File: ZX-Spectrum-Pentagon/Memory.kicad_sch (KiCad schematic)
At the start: 10 parts

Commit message: prepare for pcb
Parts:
- U31: value (none) -> 74HC32; footprint (none) -> Package_DIP:DIP-14_W7.62mm
- U34, U49: value (none) -> 74HC08; footprint (none) -> Package_DIP:DIP-14_W7.62mm
- U42, U46, U47, U48: value (none) -> 74HC257; footprint (none) -> Package_DIP:DIP-16_W7.62mm
- U43: value (none) -> 74HC541; footprint (none) -> Package_DIP:DIP-20_W7.62mm
- U44: value (none) -> HM628512; footprint (none) -> Package_DIP:DIP-32_W15.24mm
- U45: value (none) -> 74HC574; footprint (none) -> Package_DIP:DIP-20_W7.62mm
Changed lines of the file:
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@@
     (in_bom yes) (on_board yes)
     (property "Reference" "U44" (id 0) (at 109.22 20.32 0))
-    (property "Value" "" (id 1) (at 109.22 78.74 0))
-    (property "Footprint" "" (id 2) (at 109.22 20.32 0)
+    (property "Value" "HM628512" (id 1) (at 109.22 78.74 0))
+    (property "Footprint" "Package_DIP:DIP-32_W15.24mm" (id 2) (at 109.22 20.32 0)
       (effects (font (size 1.27 1.27)) hide)
     )
@@
     (in_bom yes) (on_board yes)
     (property "Reference" "U31" (id 0) (at 71.12 162.56 0))
-    (property "Value" "" (id 1) (at 71.12 170.18 0))
-    (property "Footprint" "" (id 2) (at 71.12 173.99 0)
+    (property "Value" "74HC32" (id 1) (at 71.12 170.18 0))
+    (property "Footprint" "Package_DIP:DIP-14_W7.62mm" (id 2) (at 71.12 173.99 0)
       (effects (font (size 1.27 1.27)) hide)
     )
@@
     (in_bom yes) (on_board yes)
     (property "Reference" "U43" (id 0) (at 146.05 21.59 0))
-    (property "Value" "" (id 1) (at 146.05 52.07 0))
-    (property "Footprint" "" (id 2) (at 146.05 21.59 0)
+    (property "Value" "74HC541" (id 1) (at 146.05 52.07 0))
+    (property "Footprint" "Package_DIP:DIP-20_W7.62mm" (id 2) (at 146.05 21.59 0)
       (effects (font (size 1.27 1.27)) hide)
     )
@@
     (in_bom yes) (on_board yes)
     (property "Reference" "U42" (id 0) (at 58.42 19.05 0))
-    (property "Value" "" (id 1) (at 58.42 46.99 0))
-    (property "Footprint" "" (id 2) (at 72.39 31.75 0)
+    (property "Value" "74HC257" (id 1) (at 58.42 46.99 0))
+    (property "Footprint" "Package_DIP:DIP-16_W7.62mm" (id 2) (at 72.39 31.75 0)
       (effects (font (size 1.27 1.27)) hide)
     )
@@
     (in_bom yes) (on_board yes)
     (property "Reference" "U46" (id 0) (at 58.42 57.15 0))
-    (property "Value" "" (id 1) (at 58.42 85.09 0))
-    (property "Footprint" "" (id 2) (at 72.39 69.85 0)
+    (property "Value" "74HC257" (id 1) (at 58.42 85.09 0))
+    (property "Footprint" "Package_DIP:DIP-16_W7.62mm" (id 2) (at 72.39 69.85 0)
       (effects (font (size 1.27 1.27)) hide)
     )
@@
     (in_bom yes) (on_board yes)
     (property "Reference" "U47" (id 0) (at 58.42 95.25 0))
-    (property "Value" "" (id 1) (at 58.42 123.19 0))
-    (property "Footprint" "" (id 2) (at 72.39 107.95 0)
+    (property "Value" "74HC257" (id 1) (at 58.42 123.19 0))
+    (property "Footprint" "Package_DIP:DIP-16_W7.62mm" (id 2) (at 72.39 107.95 0)
       (effects (font (size 1.27 1.27)) hide)
     )
@@
     (in_bom yes) (on_board yes)
     (property "Reference" "U48" (id 0) (at 58.42 133.35 0))
-    (property "Value" "" (id 1) (at 58.42 161.29 0))
-    (property "Footprint" "" (id 2) (at 72.39 146.05 0)
+    (property "Value" "74HC257" (id 1) (at 58.42 161.29 0))
+    (property "Footprint" "Package_DIP:DIP-16_W7.62mm" (id 2) (at 72.39 146.05 0)
       (effects (font (size 1.27 1.27)) hide)
     )
@@
     (in_bom yes) (on_board yes)
     (property "Reference" "U45" (id 0) (at 146.05 54.61 0))
-    (property "Value" "" (id 1) (at 146.05 82.55 0))
-    (property "Footprint" "" (id 2) (at 146.05 76.2 0)
+    (property "Value" "74HC574" (id 1) (at 146.05 82.55 0))
+    (property "Footprint" "Package_DIP:DIP-20_W7.62mm" (id 2) (at 146.05 76.2 0)
       (effects (font (size 1.27 1.27)) hide)
     )
@@
     (in_bom yes) (on_board yes)
     (property "Reference" "U34" (id 0) (at 71.12 172.72 0))
-    (property "Value" "" (id 1) (at 71.12 180.34 0))
-    (property "Footprint" "" (id 2) (at 71.12 184.15 0)
+    (property "Value" "74HC08" (id 1) (at 71.12 180.34 0))
+    (property "Footprint" "Package_DIP:DIP-14_W7.62mm" (id 2) (at 71.12 184.15 0)
       (effects (font (size 1.27 1.27)) hide)
     )
@@
     (in_bom yes) (on_board yes)
     (property "Reference" "U49" (id 0) (at 71.12 182.88 0))
-    (property "Value" "" (id 1) (at 71.12 190.5 0))
-    (property "Footprint" "" (id 2) (at 71.12 194.31 0)
+    (property "Value" "74HC08" (id 1) (at 71.12 190.5 0))
+    (property "Footprint" "Package_DIP:DIP-14_W7.62mm" (id 2) (at 71.12 194.31 0)
       (effects (font (size 1.27 1.27)) hide)
     )
@@
     (in_bom yes) (on_board yes)
     (property "Reference" "U34" (id 0) (at 54.61 171.45 0))
-    (property "Value" "" (id 1) (at 54.61 179.07 0))
-    (property "Footprint" "" (id 2) (at 54.61 182.88 0)
-      (effects (font (size 1.27 1.27)) hide)
-    )
+    (property "Value" "74HC08" (id 1) (at 54.61 179.07 0))
+    (property "Footprint" "Package_DIP:DIP-14_W7.62mm" (id 2) (at 54.61 182.88 0)
+      (effects (font (size 1.27 1.27)) hide)
+    )

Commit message: clear annotate
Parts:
- renumbered U44 to U?, U31 to U?, U43 to U?, U42 to U?, U46 to U?, U47 to U?, U48 to U?, U45 to U?, U34 to U?, U49 to U?
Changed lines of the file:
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@@
   (symbol (lib_id "GenericSRAM:HM628512") (at 109.22 49.53 0) (unit 1)
     (in_bom yes) (on_board yes)
-    (property "Reference" "U44" (id 0) (at 109.22 20.32 0))
+    (property "Reference" "U?" (id 0) (at 109.22 20.32 0))
     (property "Value" "HM628512" (id 1) (at 109.22 78.74 0))
     (property "Footprint" "Package_DIP:DIP-32_W15.24mm" (id 2) (at 109.22 20.32 0)
@@
   (symbol (lib_id "power:GND") (at 30.48 185.42 270) (mirror x) (unit 1)
     (in_bom yes) (on_board yes)
-    (property "Reference" "#PWR0158" (id 0) (at 24.13 185.42 0)
+    (property "Reference" "#PWR?" (id 0) (at 24.13 185.42 0)
       (effects (font (size 1.27 1.27)) hide)
     )
@@
   (symbol (lib_id "power:VCC") (at 30.48 187.96 90) (mirror x) (unit 1)
     (in_bom yes) (on_board yes)
-    (property "Reference" "#PWR0159" (id 0) (at 34.29 187.96 0)
+    (property "Reference" "#PWR?" (id 0) (at 34.29 187.96 0)
       (effects (font (size 1.27 1.27)) hide)
     )
@@
   (symbol (lib_id "74IEC:74HC32") (at 71.12 166.37 0) (unit 4)
     (in_bom yes) (on_board yes)
-    (property "Reference" "U31" (id 0) (at 71.12 162.56 0))
+    (property "Reference" "U?" (id 0) (at 71.12 162.56 0))
     (property "Value" "74HC32" (id 1) (at 71.12 170.18 0))
     (property "Footprint" "Package_DIP:DIP-14_W7.62mm" (id 2) (at 71.12 173.99 0)
@@
   (symbol (lib_id "74IEC:74HC541") (at 146.05 35.56 0) (unit 1)
     (in_bom yes) (on_board yes)
-    (property "Reference" "U43" (id 0) (at 146.05 21.59 0))
+    (property "Reference" "U?" (id 0) (at 146.05 21.59 0))
     (property "Value" "74HC541" (id 1) (at 146.05 52.07 0))
     (property "Footprint" "Package_DIP:DIP-20_W7.62mm" (id 2) (at 146.05 21.59 0)
@@
   (symbol (lib_id "74IEC:74HC257") (at 58.42 33.02 0) (unit 1)
     (in_bom yes) (on_board yes)
-    (property "Reference" "U42" (id 0) (at 58.42 19.05 0))
+    (property "Reference" "U?" (id 0) (at 58.42 19.05 0))
     (property "Value" "74HC257" (id 1) (at 58.42 46.99 0))
     (property "Footprint" "Package_DIP:DIP-16_W7.62mm" (id 2) (at 72.39 31.75 0)
@@
   (symbol (lib_id "74IEC:74HC257") (at 58.42 71.12 0) (unit 1)
     (in_bom yes) (on_board yes)
-    (property "Reference" "U46" (id 0) (at 58.42 57.15 0))
+    (property "Reference" "U?" (id 0) (at 58.42 57.15 0))
     (property "Value" "74HC257" (id 1) (at 58.42 85.09 0))
     (property "Footprint" "Package_DIP:DIP-16_W7.62mm" (id 2) (at 72.39 69.85 0)
@@
   (symbol (lib_id "74IEC:74HC257") (at 58.42 109.22 0) (unit 1)
     (in_bom yes) (on_board yes)
-    (property "Reference" "U47" (id 0) (at 58.42 95.25 0))
+    (property "Reference" "U?" (id 0) (at 58.42 95.25 0))
     (property "Value" "74HC257" (id 1) (at 58.42 123.19 0))
     (property "Footprint" "Package_DIP:DIP-16_W7.62mm" (id 2) (at 72.39 107.95 0)
@@
   (symbol (lib_id "74IEC:74HC257") (at 58.42 147.32 0) (unit 1)
     (in_bom yes) (on_board yes)
-    (property "Reference" "U48" (id 0) (at 58.42 133.35 0))
+    (property "Reference" "U?" (id 0) (at 58.42 133.35 0))
     (property "Value" "74HC257" (id 1) (at 58.42 161.29 0))
     (property "Footprint" "Package_DIP:DIP-16_W7.62mm" (id 2) (at 72.39 146.05 0)
@@
   (symbol (lib_id "74IEC:74HC574") (at 146.05 68.58 0) (unit 1)
     (in_bom yes) (on_board yes)
-    (property "Reference" "U45" (id 0) (at 146.05 54.61 0))
+    (property "Reference" "U?" (id 0) (at 146.05 54.61 0))
     (property "Value" "74HC574" (id 1) (at 146.05 82.55 0))
     (property "Footprint" "Package_DIP:DIP-20_W7.62mm" (id 2) (at 146.05 76.2 0)
@@
   (symbol (lib_id "74IEC:74HC08") (at 71.12 176.53 0) (unit 4)
     (in_bom yes) (on_board yes)
-    (property "Reference" "U34" (id 0) (at 71.12 172.72 0))
+    (property "Reference" "U?" (id 0) (at 71.12 172.72 0))
     (property "Value" "74HC08" (id 1) (at 71.12 180.34 0))
     (property "Footprint" "Package_DIP:DIP-14_W7.62mm" (id 2) (at 71.12 184.15 0)
@@
   (symbol (lib_id "74IEC:74HC08") (at 71.12 186.69 0) (unit 1)
     (in_bom yes) (on_board yes)
-    (property "Reference" "U49" (id 0) (at 71.12 182.88 0))
+    (property "Reference" "U?" (id 0) (at 71.12 182.88 0))
     (property "Value" "74HC08" (id 1) (at 71.12 190.5 0))
     (property "Footprint" "Package_DIP:DIP-14_W7.62mm" (id 2) (at 71.12 194.31 0)
@@
   (symbol (lib_id "74IEC:74HC08") (at 54.61 175.26 0) (unit 3)
     (in_bom yes) (on_board yes)
-    (property "Reference" "U34" (id 0) (at 54.61 171.45 0))
+    (property "Reference" "U?" (id 0) (at 54.61 171.45 0))
     (property "Value" "74HC08" (id 1) (at 54.61 179.07 0))
     (property "Footprint" "Package_DIP:DIP-14_W7.62mm" (id 2) (at 54.61 182.88 0)

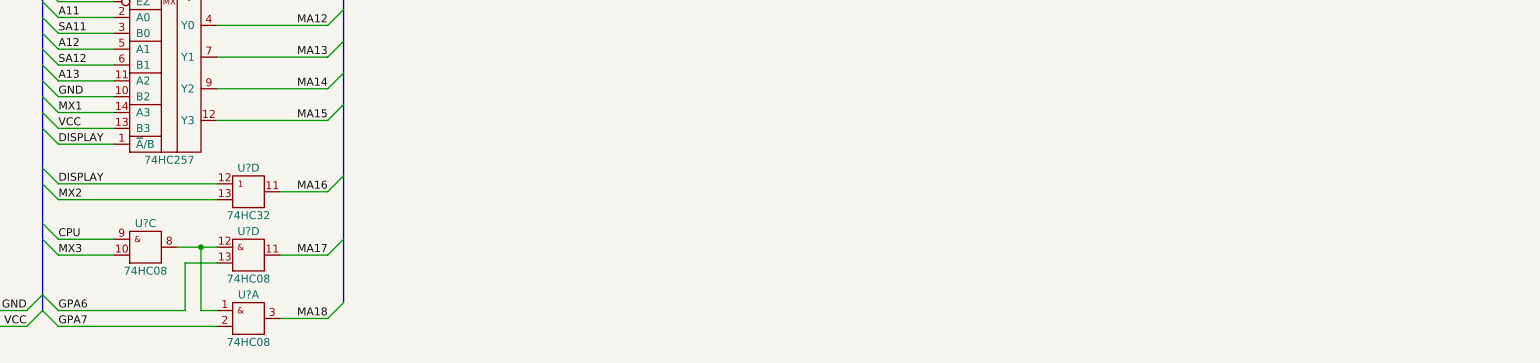
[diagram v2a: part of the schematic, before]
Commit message: reuse units of ic
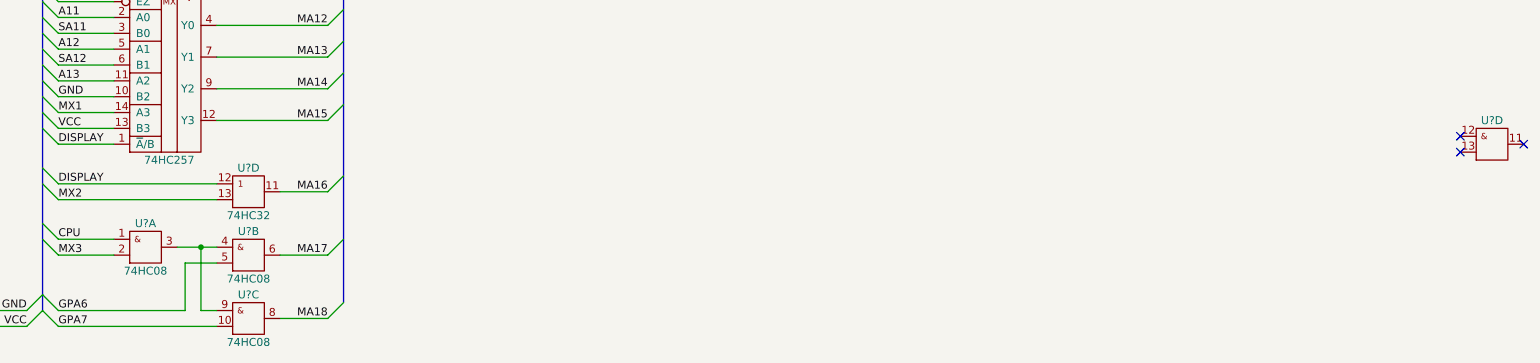
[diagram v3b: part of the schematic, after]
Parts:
- added U?: ~, symbol 74IEC:74HC08
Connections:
- net CPU: now also U?.1 (A); no longer U?.9 (A)
- net GND: now also U?.7 (GND)
- net GPA6: now also U?.5 (B); no longer U?.13 (B)
- net GPA7: now also U?.10 (B); no longer U?.2 (B)
- net MA17: now also U?.6 (~{Y}); no longer U?.11 (~{Y})
- net MA18: now also U?.8 (~{Y}); no longer U?.3 (~{Y})
- net MX3: now also U?.2 (B); no longer U?.10 (B)
- net VCC: now also U?.14 (VCC)
- new net: U?.3 (~{Y}), U?.4 (A), U?.9 (A)
- no-connect marks 0 -> 3
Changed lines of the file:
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@@
   (junction (at 127 13.97) (diameter 0) (color 0 0 0 0)
   )
+  (no_connect (at 265.43 160.02))
+  (no_connect (at 275.59 158.75))
+  (no_connect (at 265.43 157.48))
   (bus_entry (at 38.1 135.89) (size 2.54 2.54)
     (stroke (width 0) (type default) (color 0 0 0 0))
@@
     (pin "9")
   )
-  (symbol (lib_id "74IEC:74HC08") (at 71.12 176.53 0) (unit 4)
+  (symbol (lib_id "74IEC:74HC08") (at 71.12 176.53 0) (unit 2)
     (in_bom yes) (on_board yes)
     (property "Reference" "U?" (id 0) (at 71.12 172.72 0))
@@
     (pin "13")
   )
-  (symbol (lib_id "74IEC:74HC08") (at 71.12 186.69 0) (unit 1)
+  (symbol (lib_id "74IEC:74HC08") (at 71.12 186.69 0) (unit 3)
     (in_bom yes) (on_board yes)
     (property "Reference" "U?" (id 0) (at 71.12 182.88 0))
@@
     (pin "13")
   )
-  (symbol (lib_id "74IEC:74HC08") (at 54.61 175.26 0) (unit 3)
+  (symbol (lib_id "74IEC:74HC08") (at 54.61 175.26 0) (unit 1)
     (in_bom yes) (on_board yes)
     (property "Reference" "U?" (id 0) (at 54.61 171.45 0))
@@
       (effects (font (size 1.27 1.27)) hide)
     )
+    (pin "14")
+    (pin "7")
+    (pin "1")
+    (pin "2")
+    (pin "3")
+    (pin "4")
+    (pin "5")
+    (pin "6")
+    (pin "10")
+    (pin "8")
+    (pin "9")
+    (pin "11")
+    (pin "12")
+    (pin "13")
+  )
+  (symbol (lib_id "74IEC:74HC08") (at 270.51 158.75 0) (unit 4)
+    (in_bom yes) (on_board no)
+    (property "Reference" "U?" (id 0) (at 270.51 154.94 0))
+    (property "Value" "~" (id 1) (at 270.51 162.56 0))
+    (property "Footprint" "" (id 2) (at 270.51 166.37 0)
+      (effects (font (size 1.27 1.27)) hide)
+    )
+    (property "Datasheet" "https://www.ti.com/lit/ug/scyd013b/scyd013b.pdf" (id 3) (at 270.51 154.94 0)
+      (effects (font (size 1.27 1.27)) hide)
+    )

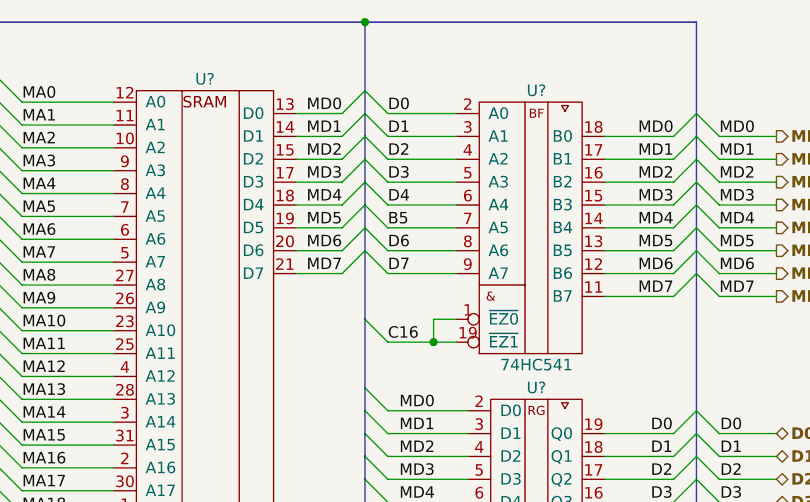
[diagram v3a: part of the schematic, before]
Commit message: revert data bus HC245 delete invertor for another direction fix line label
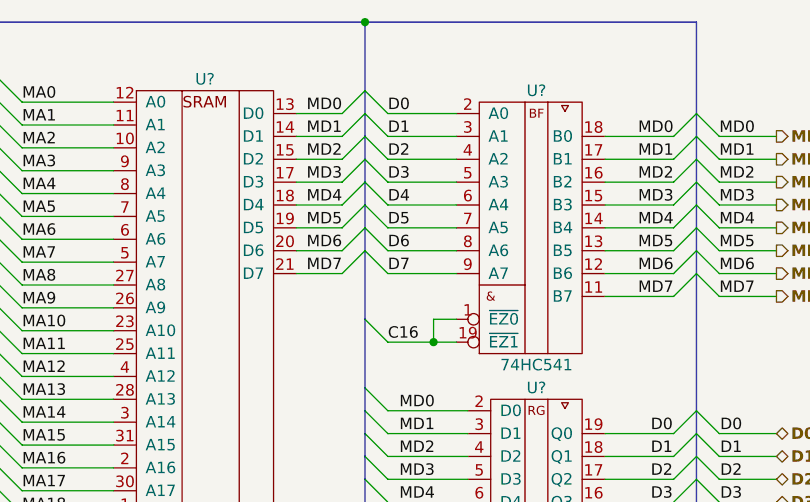
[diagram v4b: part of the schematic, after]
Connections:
- net В5 is gone; now on net D5: U?.7 (A5)
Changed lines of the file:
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@@
     (effects (font (size 1.27 1.27)) (justify left bottom))
   )
-  (label "В5" (at 129.54 36.83 0)
+  (label "D5" (at 129.54 36.83 0)
     (effects (font (size 1.27 1.27)) (justify left bottom))
   )

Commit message: annotate
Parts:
- gave numbers to parts that had none: 10
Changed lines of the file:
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@@
   (symbol (lib_id "GenericSRAM:HM628512") (at 109.22 49.53 0) (unit 1)
     (in_bom yes) (on_board yes)
-    (property "Reference" "U?" (id 0) (at 109.22 20.32 0))
+    (property "Reference" "U45" (id 0) (at 109.22 20.32 0))
     (property "Value" "HM628512" (id 1) (at 109.22 78.74 0))
     (property "Footprint" "Package_DIP:DIP-32_W15.24mm" (id 2) (at 109.22 20.32 0)
@@
   (symbol (lib_id "power:GND") (at 30.48 185.42 270) (mirror x) (unit 1)
     (in_bom yes) (on_board yes)
-    (property "Reference" "#PWR?" (id 0) (at 24.13 185.42 0)
+    (property "Reference" "#PWR059" (id 0) (at 24.13 185.42 0)
       (effects (font (size 1.27 1.27)) hide)
     )
@@
   (symbol (lib_id "power:VCC") (at 30.48 187.96 90) (mirror x) (unit 1)
     (in_bom yes) (on_board yes)
-    (property "Reference" "#PWR?" (id 0) (at 34.29 187.96 0)
+    (property "Reference" "#PWR060" (id 0) (at 34.29 187.96 0)
       (effects (font (size 1.27 1.27)) hide)
     )
@@
   (symbol (lib_id "74IEC:74HC32") (at 71.12 166.37 0) (unit 4)
     (in_bom yes) (on_board yes)
-    (property "Reference" "U?" (id 0) (at 71.12 162.56 0))
+    (property "Reference" "U31" (id 0) (at 71.12 162.56 0))
     (property "Value" "74HC32" (id 1) (at 71.12 170.18 0))
     (property "Footprint" "Package_DIP:DIP-14_W7.62mm" (id 2) (at 71.12 173.99 0)
@@
   (symbol (lib_id "74IEC:74HC541") (at 146.05 35.56 0) (unit 1)
     (in_bom yes) (on_board yes)
-    (property "Reference" "U?" (id 0) (at 146.05 21.59 0))
+    (property "Reference" "U44" (id 0) (at 146.05 21.59 0))
     (property "Value" "74HC541" (id 1) (at 146.05 52.07 0))
     (property "Footprint" "Package_DIP:DIP-20_W7.62mm" (id 2) (at 146.05 21.59 0)
@@
   (symbol (lib_id "74IEC:74HC257") (at 58.42 33.02 0) (unit 1)
     (in_bom yes) (on_board yes)
-    (property "Reference" "U?" (id 0) (at 58.42 19.05 0))
+    (property "Reference" "U43" (id 0) (at 58.42 19.05 0))
     (property "Value" "74HC257" (id 1) (at 58.42 46.99 0))
     (property "Footprint" "Package_DIP:DIP-16_W7.62mm" (id 2) (at 72.39 31.75 0)
@@
   (symbol (lib_id "74IEC:74HC257") (at 58.42 71.12 0) (unit 1)
     (in_bom yes) (on_board yes)
-    (property "Reference" "U?" (id 0) (at 58.42 57.15 0))
+    (property "Reference" "U47" (id 0) (at 58.42 57.15 0))
     (property "Value" "74HC257" (id 1) (at 58.42 85.09 0))
     (property "Footprint" "Package_DIP:DIP-16_W7.62mm" (id 2) (at 72.39 69.85 0)
@@
   (symbol (lib_id "74IEC:74HC257") (at 58.42 109.22 0) (unit 1)
     (in_bom yes) (on_board yes)
-    (property "Reference" "U?" (id 0) (at 58.42 95.25 0))
+    (property "Reference" "U48" (id 0) (at 58.42 95.25 0))
     (property "Value" "74HC257" (id 1) (at 58.42 123.19 0))
     (property "Footprint" "Package_DIP:DIP-16_W7.62mm" (id 2) (at 72.39 107.95 0)
@@
   (symbol (lib_id "74IEC:74HC257") (at 58.42 147.32 0) (unit 1)
     (in_bom yes) (on_board yes)
-    (property "Reference" "U?" (id 0) (at 58.42 133.35 0))
+    (property "Reference" "U49" (id 0) (at 58.42 133.35 0))
     (property "Value" "74HC257" (id 1) (at 58.42 161.29 0))
     (property "Footprint" "Package_DIP:DIP-16_W7.62mm" (id 2) (at 72.39 146.05 0)
@@
   (symbol (lib_id "74IEC:74HC574") (at 146.05 68.58 0) (unit 1)
     (in_bom yes) (on_board yes)
-    (property "Reference" "U?" (id 0) (at 146.05 54.61 0))
+    (property "Reference" "U46" (id 0) (at 146.05 54.61 0))
     (property "Value" "74HC574" (id 1) (at 146.05 82.55 0))
     (property "Footprint" "Package_DIP:DIP-20_W7.62mm" (id 2) (at 146.05 76.2 0)
@@
   (symbol (lib_id "74IEC:74HC08") (at 71.12 176.53 0) (unit 2)
     (in_bom yes) (on_board yes)
-    (property "Reference" "U?" (id 0) (at 71.12 172.72 0))
+    (property "Reference" "U51" (id 0) (at 71.12 172.72 0))
     (property "Value" "74HC08" (id 1) (at 71.12 180.34 0))
     (property "Footprint" "Package_DIP:DIP-14_W7.62mm" (id 2) (at 71.12 184.15 0)
@@
   (symbol (lib_id "74IEC:74HC08") (at 71.12 186.69 0) (unit 3)
     (in_bom yes) (on_board yes)
-    (property "Reference" "U?" (id 0) (at 71.12 182.88 0))
+    (property "Reference" "U51" (id 0) (at 71.12 182.88 0))
     (property "Value" "74HC08" (id 1) (at 71.12 190.5 0))
     (property "Footprint" "Package_DIP:DIP-14_W7.62mm" (id 2) (at 71.12 194.31 0)
@@
   (symbol (lib_id "74IEC:74HC08") (at 54.61 175.26 0) (unit 1)
     (in_bom yes) (on_board yes)
-    (property "Reference" "U?" (id 0) (at 54.61 171.45 0))
+    (property "Reference" "U51" (id 0) (at 54.61 171.45 0))
     (property "Value" "74HC08" (id 1) (at 54.61 179.07 0))
     (property "Footprint" "Package_DIP:DIP-14_W7.62mm" (id 2) (at 54.61 182.88 0)
@@
   (symbol (lib_id "74IEC:74HC08") (at 270.51 158.75 0) (unit 4)
     (in_bom yes) (on_board no)
-    (property "Reference" "U?" (id 0) (at 270.51 154.94 0))
+    (property "Reference" "U50" (id 0) (at 270.51 154.94 0))
     (property "Value" "~" (id 1) (at 270.51 162.56 0))
     (property "Footprint" "" (id 2) (at 270.51 166.37 0)
